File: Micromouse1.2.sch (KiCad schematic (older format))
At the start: 0 parts

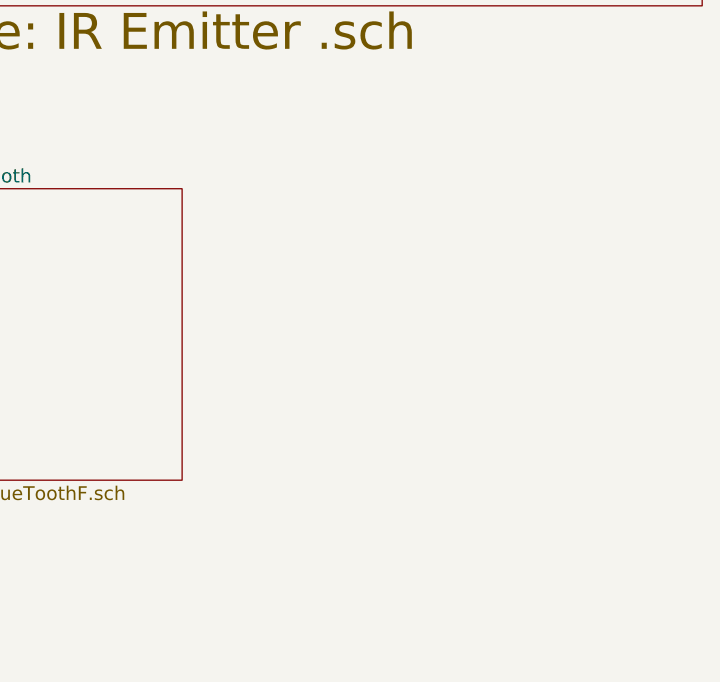
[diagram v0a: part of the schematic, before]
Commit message: Added MPU-6500
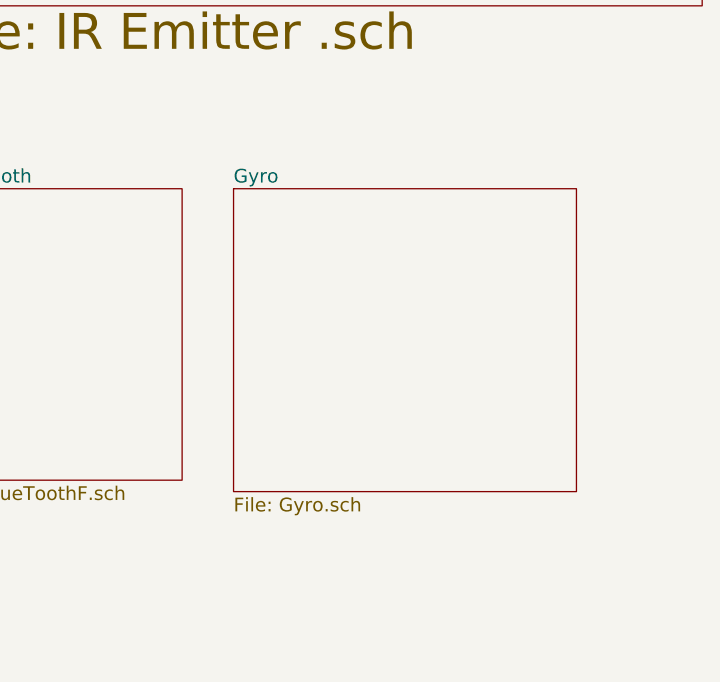
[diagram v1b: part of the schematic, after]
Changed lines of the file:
@@
 EESchema Schematic File Version 2
+LIBS:device
+LIBS:Micromouse
 LIBS:power
-LIBS:device
 LIBS:transistors
 LIBS:conn
@@
 LIBS:contrib
 LIBS:valves
-LIBS:Micromouse
 LIBS:1_PJC-Sandbox
 LIBS:Micromouse1.2-cache
@@
 $Descr A4 11693 8268
 encoding utf-8
-Sheet 1 7
+Sheet 1 8
 Title ""
 Date ""
@@
 F1 "BlueToothF.sch" 60
 $EndSheet
+$Sheet
+S 8625 3450 1500 1325
+U 59AB6D77
+F0 "Gyro" 60
+F1 "Gyro.sch" 60
+$EndSheet
 $EndSCHEMATC

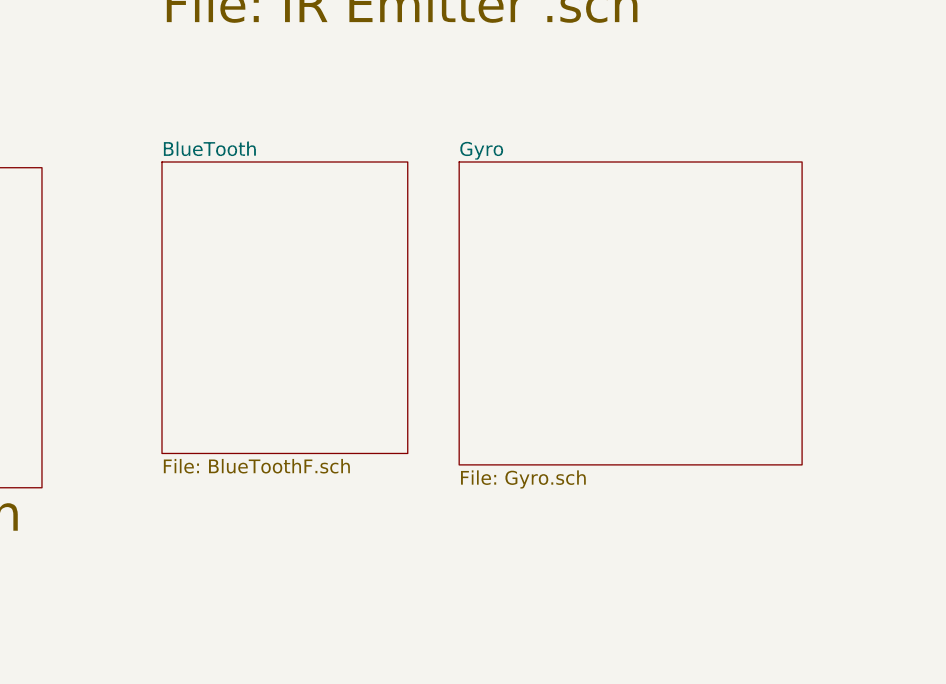
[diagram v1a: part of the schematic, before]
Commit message: finished floor planning
-replaced the TC4427 and H brige by a single DRV8833 chip
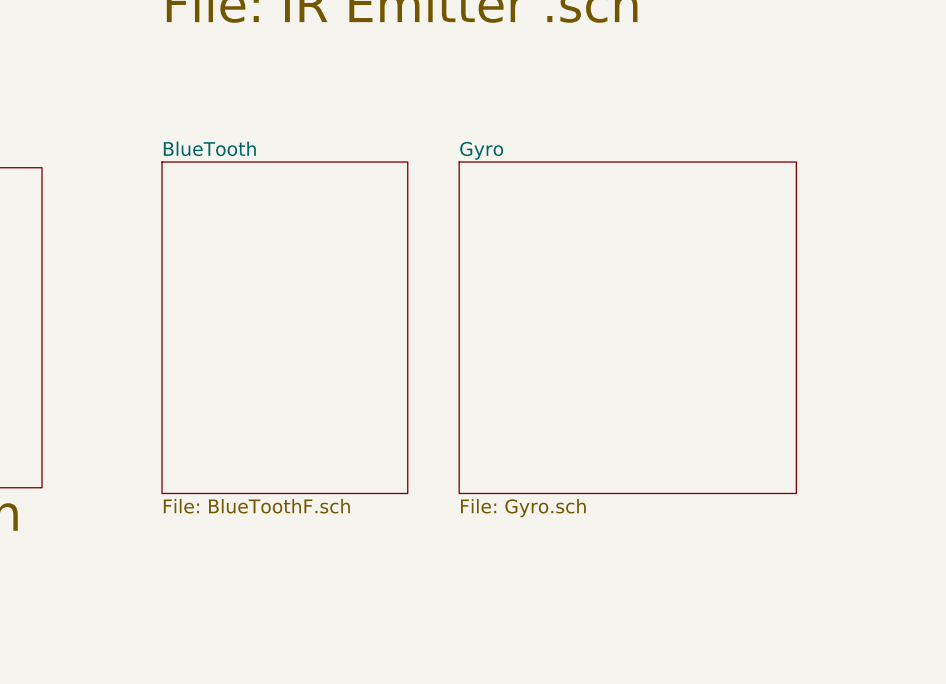
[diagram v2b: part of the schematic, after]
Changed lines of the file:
@@
 EESchema Schematic File Version 2
+LIBS:1_PJC-Sandbox
+LIBS:Micromouse1.2-rescue
+LIBS:Micromouse1.2-cache
+LIBS:74xgxx
+LIBS:74xx
+LIBS:ac-dc
+LIBS:actel
+LIBS:adc-dac
+LIBS:allegro
+LIBS:Altera
+LIBS:analog_devices
+LIBS:analog_switches
+LIBS:atmel
+LIBS:audio
+LIBS:battery_management
+LIBS:bbd
+LIBS:bosch
+LIBS:brooktre
+LIBS:cmos_ieee
+LIBS:cmos4000
+LIBS:conn
+LIBS:contrib
+LIBS:cypress
+LIBS:dc-dc
 LIBS:device
-LIBS:Micromouse
+LIBS:digital-audio
+LIBS:diode
+LIBS:display
+LIBS:dsp
+LIBS:elec-unifil
+LIBS:ESD_Protection
+LIBS:ftdi
+LIBS:gennum
+LIBS:graphic
+LIBS:hc11
+LIBS:intel
+LIBS:interface
+LIBS:ir
+LIBS:Lattice
+LIBS:leds
+LIBS:linear
+LIBS:logo
+LIBS:maxim
+LIBS:mechanical
+LIBS:memory
+LIBS:microchip
+LIBS:microchip_dspic33dsc
+LIBS:microchip_pic10mcu
+LIBS:microchip_pic12mcu
+LIBS:microchip_pic16mcu
+LIBS:microchip_pic18mcu
+LIBS:microchip_pic24mcu
+LIBS:microchip_pic32mcu
+LIBS:microcontrollers
+LIBS:modules
+LIBS:motor_drivers
+LIBS:motorola
+LIBS:motors
+LIBS:msp430
+LIBS:nordicsemi
+LIBS:nxp
+LIBS:nxp_armmcu
+LIBS:onsemi
+LIBS:opto
+LIBS:Oscillators
+LIBS:philips
 LIBS:power
+LIBS:Power_Management
+LIBS:powerint
+LIBS:pspice
+LIBS:references
+LIBS:regul
+LIBS:relays
+LIBS:rfcom
+LIBS:sensors
+LIBS:silabs
+LIBS:siliconi
+LIBS:stm8
+LIBS:stm32
+LIBS:supertex
+LIBS:switches
+LIBS:texas
+LIBS:transf
 LIBS:transistors
-LIBS:conn
-LIBS:linear
-LIBS:regul
-LIBS:74xx
-LIBS:cmos4000
-LIBS:adc-dac
-LIBS:memory
+LIBS:triac_thyristor
+LIBS:ttl_ieee
+LIBS:valves
+LIBS:video
+LIBS:wiznet
+LIBS:Worldsemi
+LIBS:Xicor
 LIBS:xilinx
-LIBS:microcontrollers
-LIBS:dsp
-LIBS:microchip
-LIBS:analog_switches
-LIBS:motorola
-LIBS:texas
-LIBS:intel
-LIBS:audio
-LIBS:interface
-LIBS:digital-audio
-LIBS:philips
-LIBS:display
-LIBS:cypress
-LIBS:siliconi
-LIBS:opto
-LIBS:atmel
-LIBS:contrib
-LIBS:valves
-LIBS:1_PJC-Sandbox
-LIBS:Micromouse1.2-cache
+LIBS:zetex
+LIBS:Zilog
 EELAYER 25 0
 EELAYER END
@@
 $EndSheet
 $Sheet
-S 7325 3450 1075 1275
+S 7325 3450 1075 1450
 U 597FE5C0
 F0 "BlueTooth" 60
@@
 $EndSheet
 $Sheet
-S 8625 3450 1500 1325
+S 8625 3450 1475 1450
 U 59AB6D77
 F0 "Gyro" 60
